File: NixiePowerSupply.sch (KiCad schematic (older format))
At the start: 22 parts, among them J1 BARREL_JACK, J2 CONN_01X04, J3 CONN_01X05, Q1 2SA1015, Q2 2SK3234, U1 NJM2360, U2 7805

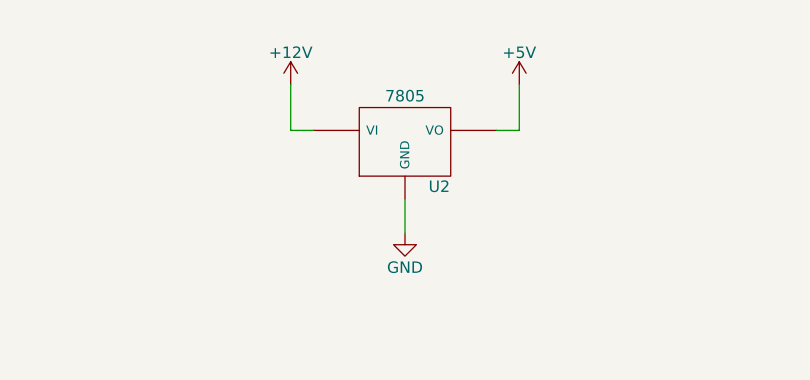
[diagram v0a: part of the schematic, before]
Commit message: Placement & Trace layoit done
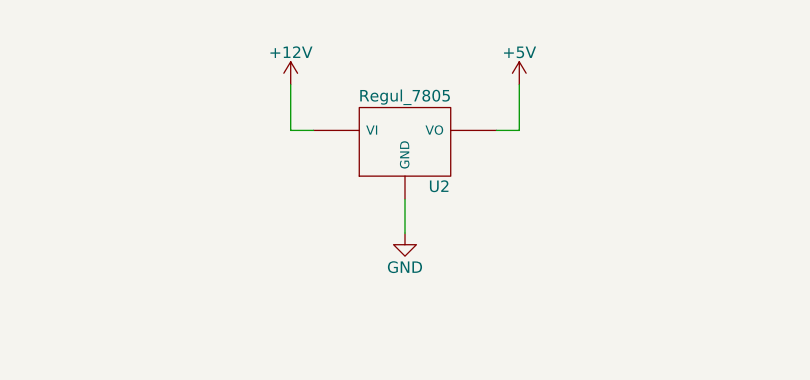
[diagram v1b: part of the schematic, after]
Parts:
- removed U2: 7805, TO_SOT_Packages_THT:TO-220-3_Vertical, symbol 7805
- added U2: Regul_7805, TO_SOT_Packages_THT:TO-220-3_Vertical, symbol Regul_7805
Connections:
- net +12V: now also U2.1 (VI)
- net +5V: now also U2.3 (VO)
- net GND: now also U2.2 (GND)
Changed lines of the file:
@@
 	7950 4450 7950 4700
-$Comp
-L 7805 U2
-U 1 1 59DCB4BF
-P 5600 1900
-F 0 "U2" H 5750 1704 50  0000 C CNN
-F 1 "7805" H 5600 2100 50  0000 C CNN
-F 2 "TO_SOT_Packages_THT:TO-220-3_Vertical" H 5600 1900 50  0001 C CNN
-F 3 "" H 5600 1900 50  0001 C CNN
-	1    5600 1900
-	1    0    0    -1
-$EndComp
 $Comp
 L BARREL_JACK J1
@@
 	8100 4900 7950 4900
 Connection ~ 7950 5000
+$Comp
+L Regul_7805 U2
+U 1 1 59E6DCCE
+P 5600 1900
+F 0 "U2" H 5750 1704 50  0000 C CNN
+F 1 "Regul_7805" H 5600 2100 50  0000 C CNN
+F 2 "TO_SOT_Packages_THT:TO-220-3_Vertical" H 5600 1900 50  0001 C CNN
+F 3 "" H 5600 1900 50  0001 C CNN
+	1    5600 1900
+	1    0    0    -1
+$EndComp
 $EndSCHEMATC
